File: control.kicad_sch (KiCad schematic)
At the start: 7 parts

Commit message: [#72133] Unify sheet size
Signed-off-by: Dawid Lentka <dlentka@antmicro.com>
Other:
- title: (none) -> LED Panel Board
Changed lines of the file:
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@@
 	(generator_version "8.0")
 	(paper "A4")
+	(title_block
+		(title "LED Panel Board")
+		(date "28.01.2025")
+		(rev "1.0.0")
+	)
 	(junction
 		(at 128.27 142.24)

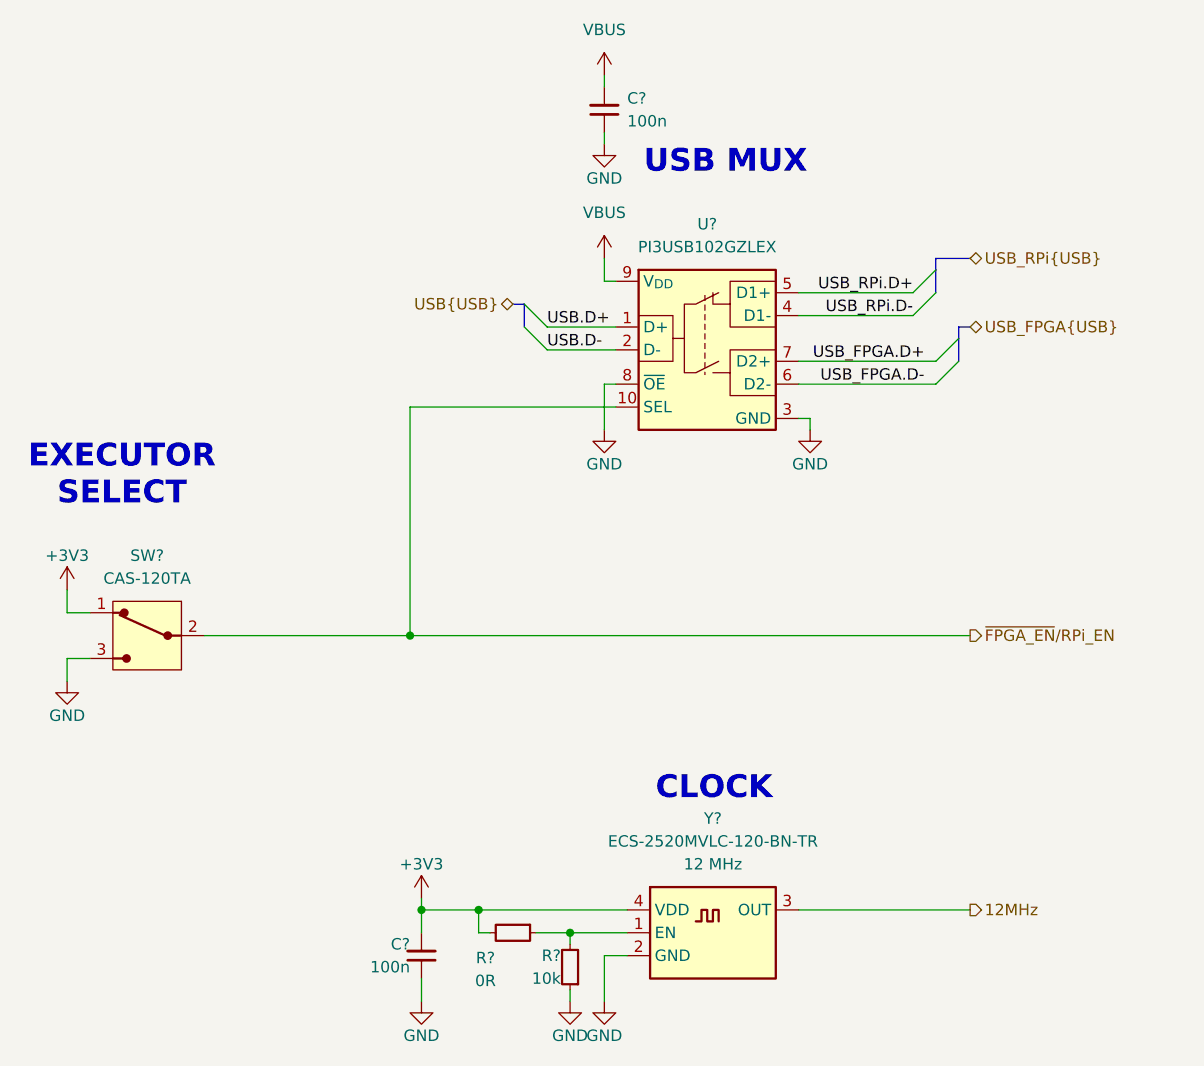
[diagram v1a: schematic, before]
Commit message: [#72133] Add indicator LEDs & testpoints
Signed-off-by: Dawid Lentka <dlentka@antmicro.com>
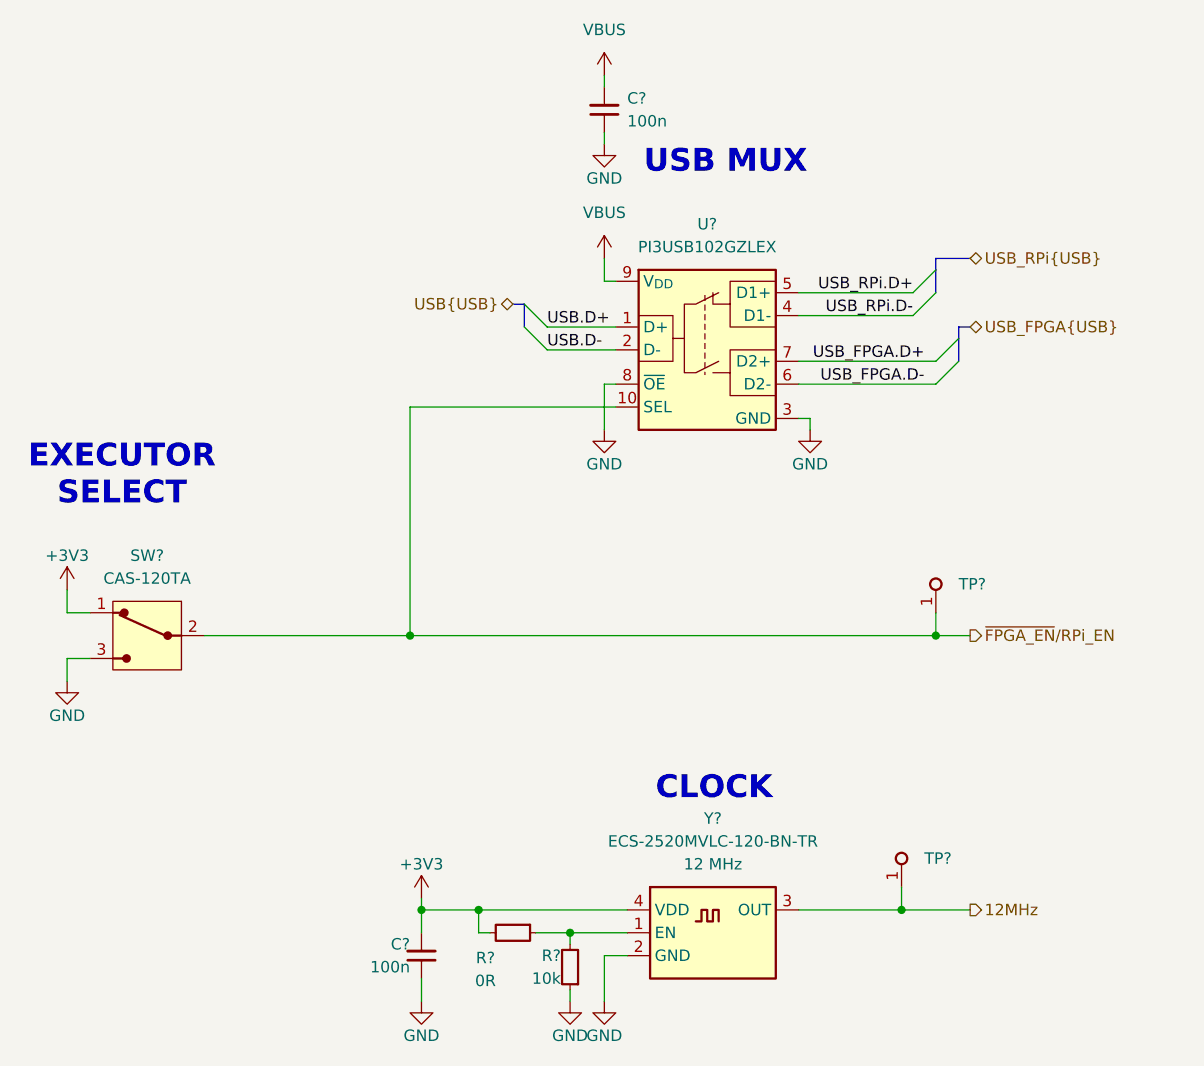
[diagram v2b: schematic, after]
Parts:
- added TP? (x2): TP_0.75mm_SMD, antmicro-footprints:TP_SMD_0.75mm, symbol antmicroTestPoints:TP_0.75mm_SMD
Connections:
- net 12MHz: now also TP?.1
- net ~{FPGA_EN}/RPi_EN: now also TP?.1

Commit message: [#72133] Annotate schematics
Signed-off-by: Dawid Lentka <dlentka@antmicro.com>
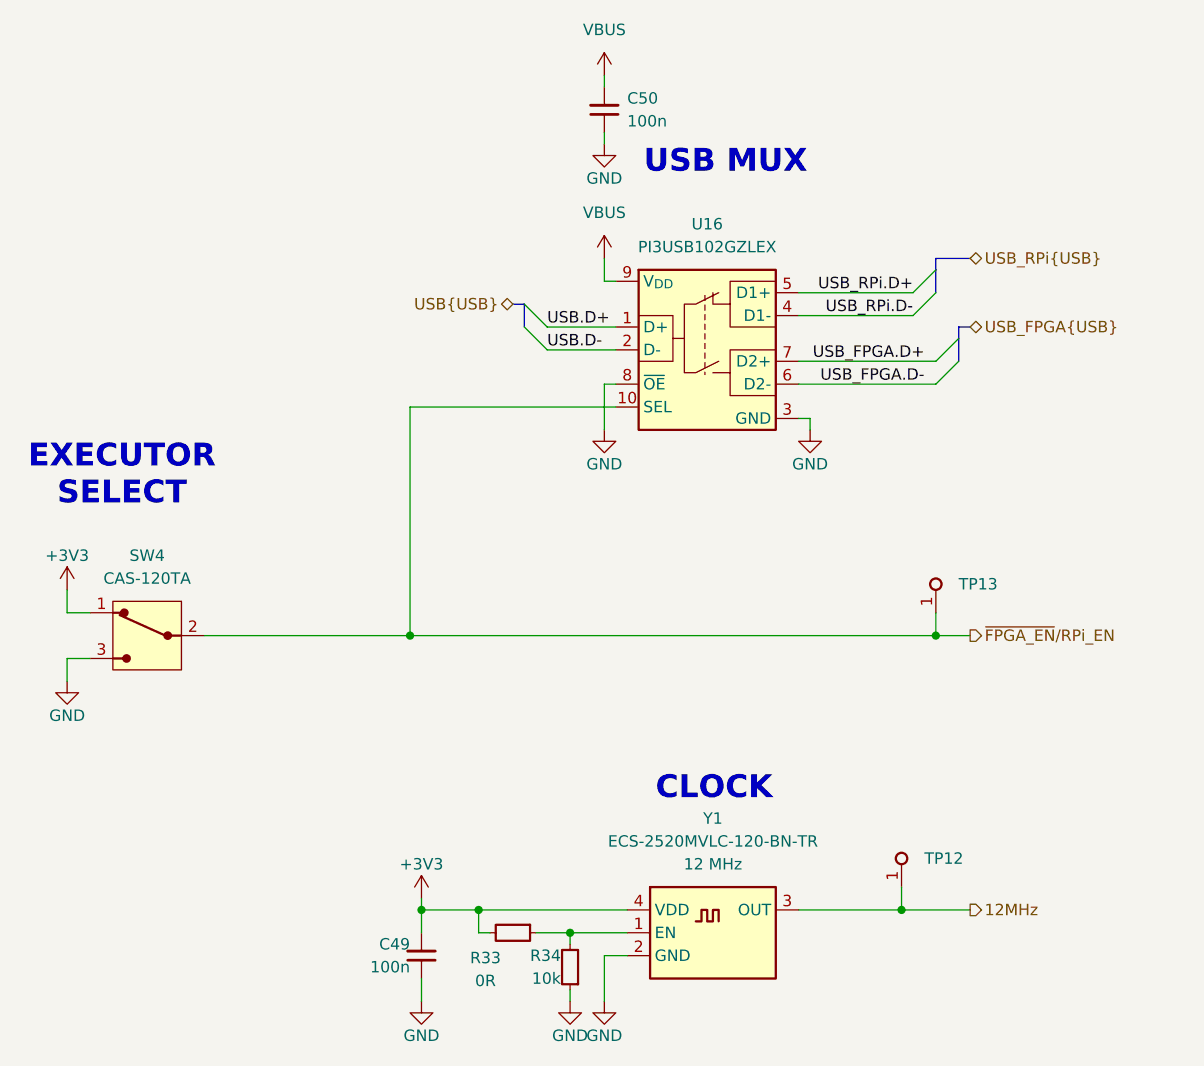
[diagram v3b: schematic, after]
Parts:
- gave numbers to parts that had none: 9
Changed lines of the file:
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@@
 		(dnp no)
 		(fields_autoplaced yes)
-		(property "Reference" "C?"
+		(property "Reference" "C50"
 			(at 144.78 52.0636 90)
 			(effects
@@
 			(project "led-panel"
 				(path "/a86e1cab-ea0a-45e6-9194-d44b0d5c9450/db63d7f0-b7b2-40ed-85ed-c3224adc3539"
-					(reference "C?")
+					(reference "C50")
 					(unit 1)
 				)
@@
 		(on_board yes)
 		(dnp no)
-		(property "Reference" "#PWR095"
+		(property "Reference" "#PWR0122"
 			(at 133.35 91.44 0)
 			(effects
@@
 			(project "led-panel"
 				(path "/a86e1cab-ea0a-45e6-9194-d44b0d5c9450/db63d7f0-b7b2-40ed-85ed-c3224adc3539"
-					(reference "#PWR095")
+					(reference "#PWR0122")
 					(unit 1)
 				)
@@
 		(dnp no)
 		(fields_autoplaced yes)
-		(property "Reference" "TP?"
+		(property "Reference" "TP13"
 			(at 181.61 106.045 90)
 			(effects
@@
 			(project "led-panel"
 				(path "/a86e1cab-ea0a-45e6-9194-d44b0d5c9450/db63d7f0-b7b2-40ed-85ed-c3224adc3539"
-					(reference "TP?")
+					(reference "TP13")
 					(unit 1)
 				)
@@
 		(on_board yes)
 		(dnp no)
-		(property "Reference" "#PWR026"
+		(property "Reference" "#PWR0123"
 			(at 133.35 154.94 0)
 			(effects
@@
 			(project "led-panel"
 				(path "/a86e1cab-ea0a-45e6-9194-d44b0d5c9450/db63d7f0-b7b2-40ed-85ed-c3224adc3539"
-					(reference "#PWR026")
+					(reference "#PWR0123")
 					(unit 1)
 				)
@@
 		(dnp no)
 		(fields_autoplaced yes)
-		(property "Reference" "SW?"
+		(property "Reference" "SW4"
 			(at 91.44 102.87 0)
 			(effects
@@
 			(project "led-panel"
 				(path "/a86e1cab-ea0a-45e6-9194-d44b0d5c9450/db63d7f0-b7b2-40ed-85ed-c3224adc3539"
-					(reference "SW?")
+					(reference "SW4")
 					(unit 1)
 				)
@@
 		(on_board yes)
 		(dnp no)
-		(property "Reference" "#PWR015"
+		(property "Reference" "#PWR0116"
 			(at 137.16 140.97 0)
 			(effects
@@
 			(project "led-panel"
 				(path "/a86e1cab-ea0a-45e6-9194-d44b0d5c9450/db63d7f0-b7b2-40ed-85ed-c3224adc3539"
-					(reference "#PWR015")
+					(reference "#PWR0116")
 					(unit 1)
 				)
@@
 		(dnp no)
 		(fields_autoplaced yes)
-		(property "Reference" "Y?"
+		(property "Reference" "Y1"
 			(at 154.305 132.08 0)
 			(effects
@@
 			(project "led-panel"
 				(path "/a86e1cab-ea0a-45e6-9194-d44b0d5c9450/db63d7f0-b7b2-40ed-85ed-c3224adc3539"
-					(reference "Y?")
+					(reference "Y1")
 					(unit 1)
 				)
@@
 		(on_board yes)
 		(dnp no)
-		(property "Reference" "#PWR093"
+		(property "Reference" "#PWR0120"
 			(at 151.13 59.69 0)
 			(effects
@@
 			(project "led-panel"
 				(path "/a86e1cab-ea0a-45e6-9194-d44b0d5c9450/db63d7f0-b7b2-40ed-85ed-c3224adc3539"
-					(reference "#PWR093")
+					(reference "#PWR0120")
 					(unit 1)
 				)
@@
 		(dnp no)
 		(fields_autoplaced yes)
-		(property "Reference" "#PWR094"
+		(property "Reference" "#PWR0121"
 			(at 142.24 73.66 0)
 			(effects
@@
 			(project "led-panel"
 				(path "/a86e1cab-ea0a-45e6-9194-d44b0d5c9450/db63d7f0-b7b2-40ed-85ed-c3224adc3539"
-					(reference "#PWR094")
+					(reference "#PWR0121")
 					(unit 1)
 				)
@@
 		(on_board yes)
 		(dnp no)
-		(property "Reference" "#PWR020"
+		(property "Reference" "#PWR0118"
 			(at 129.54 154.94 0)
 			(effects
@@
 			(project "led-panel"
 				(path "/a86e1cab-ea0a-45e6-9194-d44b0d5c9450/db63d7f0-b7b2-40ed-85ed-c3224adc3539"
-					(reference "#PWR020")
+					(reference "#PWR0118")
 					(unit 1)
 				)
@@
 		(dnp no)
 		(fields_autoplaced yes)
-		(property "Reference" "U?"
+		(property "Reference" "U16"
 			(at 153.67 66.04 0)
 			(effects
@@
 			(project "led-panel"
 				(path "/a86e1cab-ea0a-45e6-9194-d44b0d5c9450/db63d7f0-b7b2-40ed-85ed-c3224adc3539"
-					(reference "U?")
+					(reference "U16")
 					(unit 1)
 				)
@@
 		(on_board yes)
 		(dnp no)
-		(property "Reference" "#PWR019"
+		(property "Reference" "#PWR0117"
 			(at 113.03 154.94 0)
 			(effects
@@
 			(project "led-panel"
 				(path "/a86e1cab-ea0a-45e6-9194-d44b0d5c9450/db63d7f0-b7b2-40ed-85ed-c3224adc3539"
-					(reference "#PWR019")
+					(reference "#PWR0117")
 					(unit 1)
 				)
@@
 		(on_board yes)
 		(dnp no)
-		(property "Reference" "R?"
+		(property "Reference" "R34"
 			(at 137.414 147.32 90)
 			(effects
@@
 			(project "led-panel"
 				(path "/a86e1cab-ea0a-45e6-9194-d44b0d5c9450/db63d7f0-b7b2-40ed-85ed-c3224adc3539"
-					(reference "R?")
+					(reference "R34")
 					(unit 1)
 				)
@@
 		(on_board yes)
 		(dnp no)
-		(property "Reference" "#PWR091"
+		(property "Reference" "#PWR0115"
 			(at 73.66 119.38 0)
 			(effects
@@
 			(project "led-panel"
 				(path "/a86e1cab-ea0a-45e6-9194-d44b0d5c9450/db63d7f0-b7b2-40ed-85ed-c3224adc3539"
-					(reference "#PWR091")
+					(reference "#PWR0115")
 					(unit 1)
 				)
@@
 		(on_board yes)
 		(dnp no)
-		(property "Reference" "#PWR096"
+		(property "Reference" "#PWR0124"
 			(at 156.21 91.44 0)
 			(effects
@@
 			(project "led-panel"
 				(path "/a86e1cab-ea0a-45e6-9194-d44b0d5c9450/db63d7f0-b7b2-40ed-85ed-c3224adc3539"
-					(reference "#PWR096")
+					(reference "#PWR0124")
 					(unit 1)
 				)
@@
 		(dnp no)
 		(fields_autoplaced yes)
-		(property "Reference" "TP?"
+		(property "Reference" "TP12"
 			(at 177.8 136.525 90)
 			(effects
@@
 			(project "led-panel"
 				(path "/a86e1cab-ea0a-45e6-9194-d44b0d5c9450/db63d7f0-b7b2-40ed-85ed-c3224adc3539"
-					(reference "TP?")
+					(reference "TP12")
 					(unit 1)
 				)
@@
 		(on_board yes)
 		(dnp no)
-		(property "Reference" "R?"
+		(property "Reference" "R33"
 			(at 129.032 147.574 0)
 			(effects
@@
 			(project "led-panel"
 				(path "/a86e1cab-ea0a-45e6-9194-d44b0d5c9450/db63d7f0-b7b2-40ed-85ed-c3224adc3539"
-					(reference "R?")
+					(reference "R33")
 					(unit 1)
 				)
@@
 		(dnp no)
 		(fields_autoplaced yes)
-		(property "Reference" "#PWR092"
+		(property "Reference" "#PWR0119"
 			(at 142.24 53.34 0)
 			(effects
@@
 			(project "led-panel"
 				(path "/a86e1cab-ea0a-45e6-9194-d44b0d5c9450/db63d7f0-b7b2-40ed-85ed-c3224adc3539"
-					(reference "#PWR092")
+					(reference "#PWR0119")
 					(unit 1)
 				)
@@
 		(on_board yes)
 		(dnp no)
-		(property "Reference" "C?"
+		(property "Reference" "C49"
 			(at 120.65 146.05 90)
 			(effects
@@
 			(project "led-panel"
 				(path "/a86e1cab-ea0a-45e6-9194-d44b0d5c9450/db63d7f0-b7b2-40ed-85ed-c3224adc3539"
-					(reference "C?")
+					(reference "C49")
 					(unit 1)
 				)
@@
 		(on_board yes)
 		(dnp no)
-		(property "Reference" "#PWR089"
+		(property "Reference" "#PWR0114"
 			(at 97.79 106.68 0)
 			(effects
@@
 			(project "led-panel"
 				(path "/a86e1cab-ea0a-45e6-9194-d44b0d5c9450/db63d7f0-b7b2-40ed-85ed-c3224adc3539"
-					(reference "#PWR089")
+					(reference "#PWR0114")
 					(unit 1)
 				)

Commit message: [#72133] Sch: Update control hierarchy
Signed-off-by: Dawid Lentka <dlentka@antmicro.com>
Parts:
- removed C49, C50: C_100n_0402, antmicro-footprints:C_0402_1005Metric, symbol antmicroCapacitors0402:C_100n_0402
- removed R33: R_0R_0402, antmicro-footprints:R_0402_1005Metric, symbol antmicroResistors0402:R_0R_0402
- removed R34: R_10k_0402, antmicro-footprints:R_0402_1005Metric, symbol antmicroResistors0402:R_10k_0402
- removed SW4: CAS-120TA, antmicro-footprints:Switch_Slide_CAS-120TA, symbol antmicroSlideSwitches:CAS-120TA
- removed TP12, TP13: TP_0.75mm_SMD, antmicro-footprints:TP_SMD_0.75mm, symbol antmicroTestPoints:TP_0.75mm_SMD
- removed U16: PI3USB102GZLEX, antmicro-footprints:UQFN-10_1.4x1.8x0.5mm_P0.4mm, symbol antmicroInterfaceAnalogSwitchesSpecialPurpose:PI3USB102GZLEX
- removed Y1: Oscillator_12MHz_ESC_2520MV, antmicro-footprints:Oscillator_SMD_ECS_2520MV_2.5x2mm, symbol antmicroOscillators:Oscillator_12MHz_ESC_2520MV
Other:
- note removed: "CLOCK"
- note removed: "EXECUTOR SELECT"
- note removed: "USB MUX"
